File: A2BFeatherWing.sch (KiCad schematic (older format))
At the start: 2 parts, among them J1 Conn_01x04_Male, U1 FeatherWingTemplate

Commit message: added datasheets, power
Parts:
- U1: symbol Knochi_Modules:FeatherWingTemplate -> A2BFeatherWing-rescue:FeatherWingTemplate-Knochi_Modules
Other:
- note added: "* Feather M0 - either rx or tx\n * WS connected to pin 0 \n * CLK connected to pin 1\n * SD connected to pin 9"
- note added: "* Feather M4 - simultaneous rx and tx\n * WS connected to pin 0\n * CLK connected to pin 1\n * SDI connected to pin 12\n * SDO connected to pin 11"
- moved on the sheet: J1
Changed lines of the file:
@@
 $EndDescr
 $Comp
-L Knochi_Modules:FeatherWingTemplate U1
+L A2BFeatherWing-rescue:FeatherWingTemplate-Knochi_Modules U1
 U 1 1 5DC48552
 P 2000 6000
@@
 $EndComp
 $Sheet
-S 6200 2600 1450 1300
+S 5975 2725 1375 1650
 U 5DC4BC55
 F0 "A2B" 50
 F1 "A2BFeatherWing_A2B.sch" 50
+F2 "BN" O R 7350 3175 50
+F3 "BP" O R 7350 3275 50
+F4 "AN" O R 7350 3475 50
+F5 "AP" O R 7350 3375 50
+F6 "SCL" I L 5975 3000 50
+F7 "SDA" B L 5975 3125 50
+F8 "BCLK" I L 5975 3325 50
+F9 "SYNC" I L 5975 3450 50
+F10 "IO0" B L 5975 3575 50
+F11 "IO1" B L 5975 3650 50
+F12 "IO2" B L 5975 3750 50
+F13 "IO3" B L 5975 3800 50
+F14 "IO4" B L 5975 3925 50
+F15 "IO5" B L 5975 3900 50
+F16 "IO6" B L 5975 3975 50
+F17 "IO7" B L 5975 3850 50
 $EndSheet
 $Comp
 L Connector:Conn_01x04_Male J1
 U 1 1 5DC5628E
-P 9000 3250
-F 0 "J1" H 8972 3132 50  0000 R CNN
-F 1 "Conn_01x04_Male" H 8972 3223 50  0000 R CNN
-F 2 "Connector_JST:JST_PH_S4B-PH-SM4-TB_1x04-1MP_P2.00mm_Horizontal" H 9000 3250 50  0001 C CNN
-F 3 "~" H 9000 3250 50  0001 C CNN
-	1    9000 3250
+P 9000 3375
+F 0 "J1" H 8972 3257 50  0000 R CNN
+F 1 "Conn_01x04_Male" H 8972 3348 50  0000 R CNN
+F 2 "Connector_JST:JST_PH_S4B-PH-SM4-TB_1x04-1MP_P2.00mm_Horizontal" H 9000 3375 50  0001 C CNN
+F 3 "~" H 9000 3375 50  0001 C CNN
+	1    9000 3375
 	-1   0    0    1
 $EndComp
@@
 F1 "A2BFeatherWing_PWR.sch" 50
 $EndSheet
+Text Notes 2925 7100 0    50   ~ 0
+ * Feather M0 - either rx or tx\n   * WS connected to pin 0 \n   * CLK connected to pin 1\n   * SD connected to pin 9
+Text Notes 2975 6425 0    50   ~ 0
+* Feather M4 - simultaneous rx and tx\n  * WS connected to pin 0\n  * CLK connected to pin 1\n  * SDI connected to pin 12\n  * SDO connected to pin 11
 $EndSCHEMATC

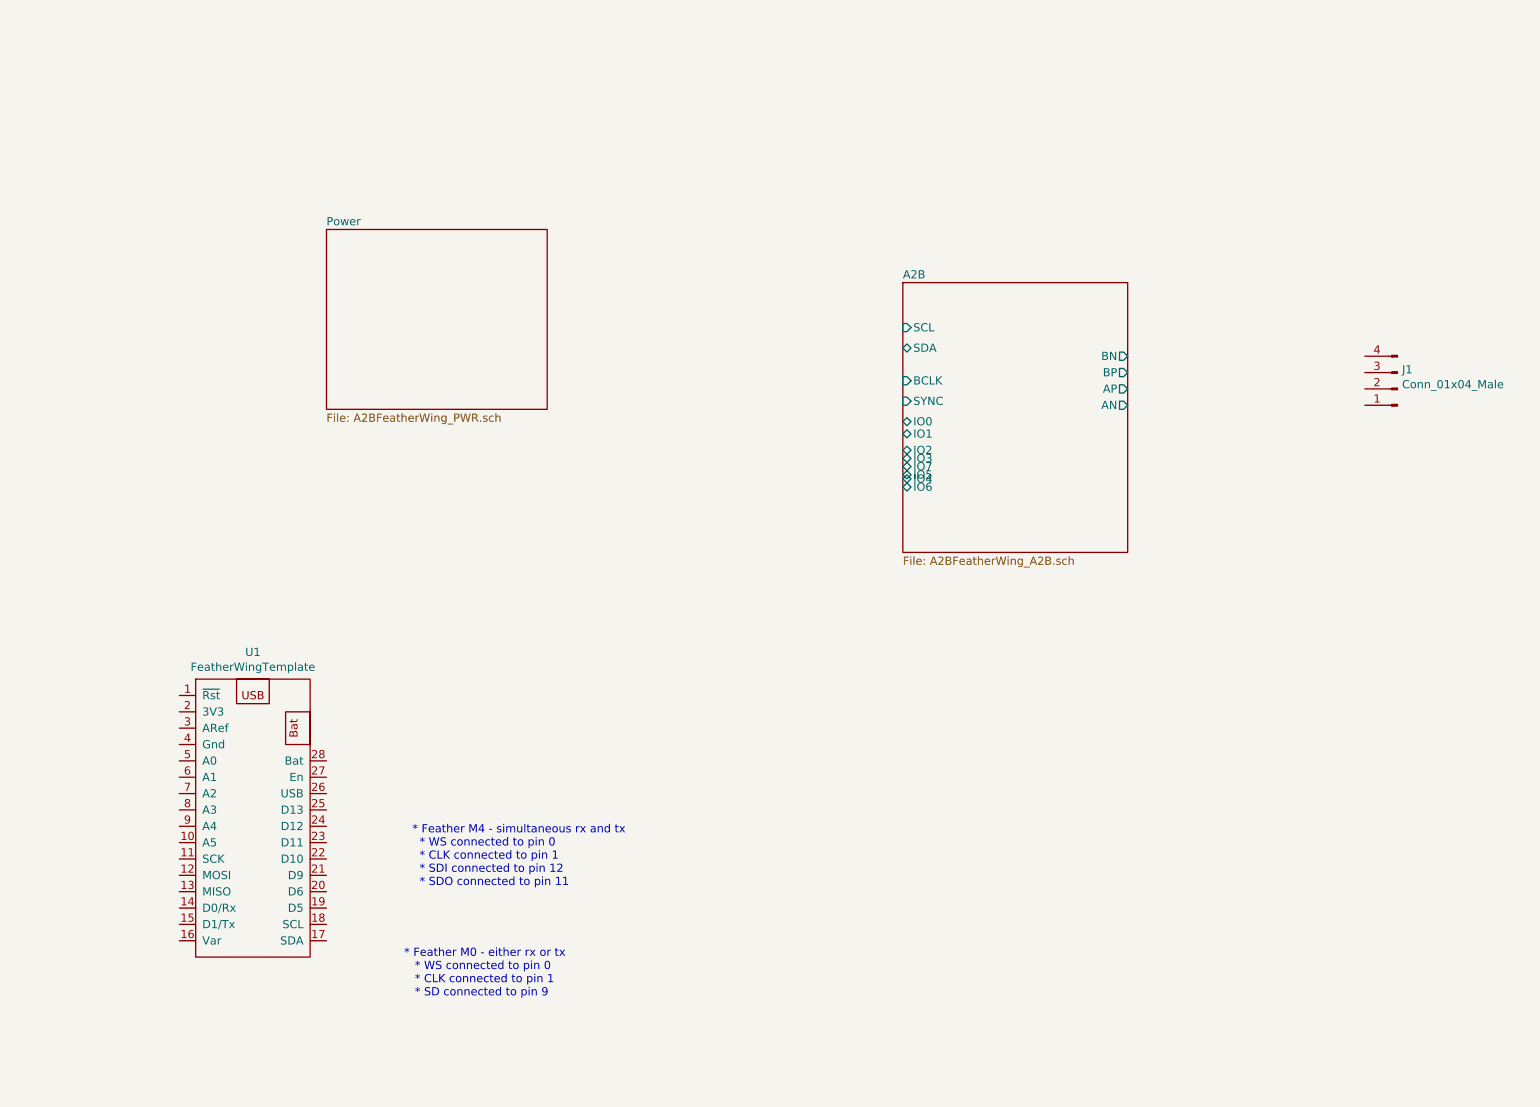
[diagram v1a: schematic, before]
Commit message: added 3d model of JST PH and CM added eco layer for silkscreen
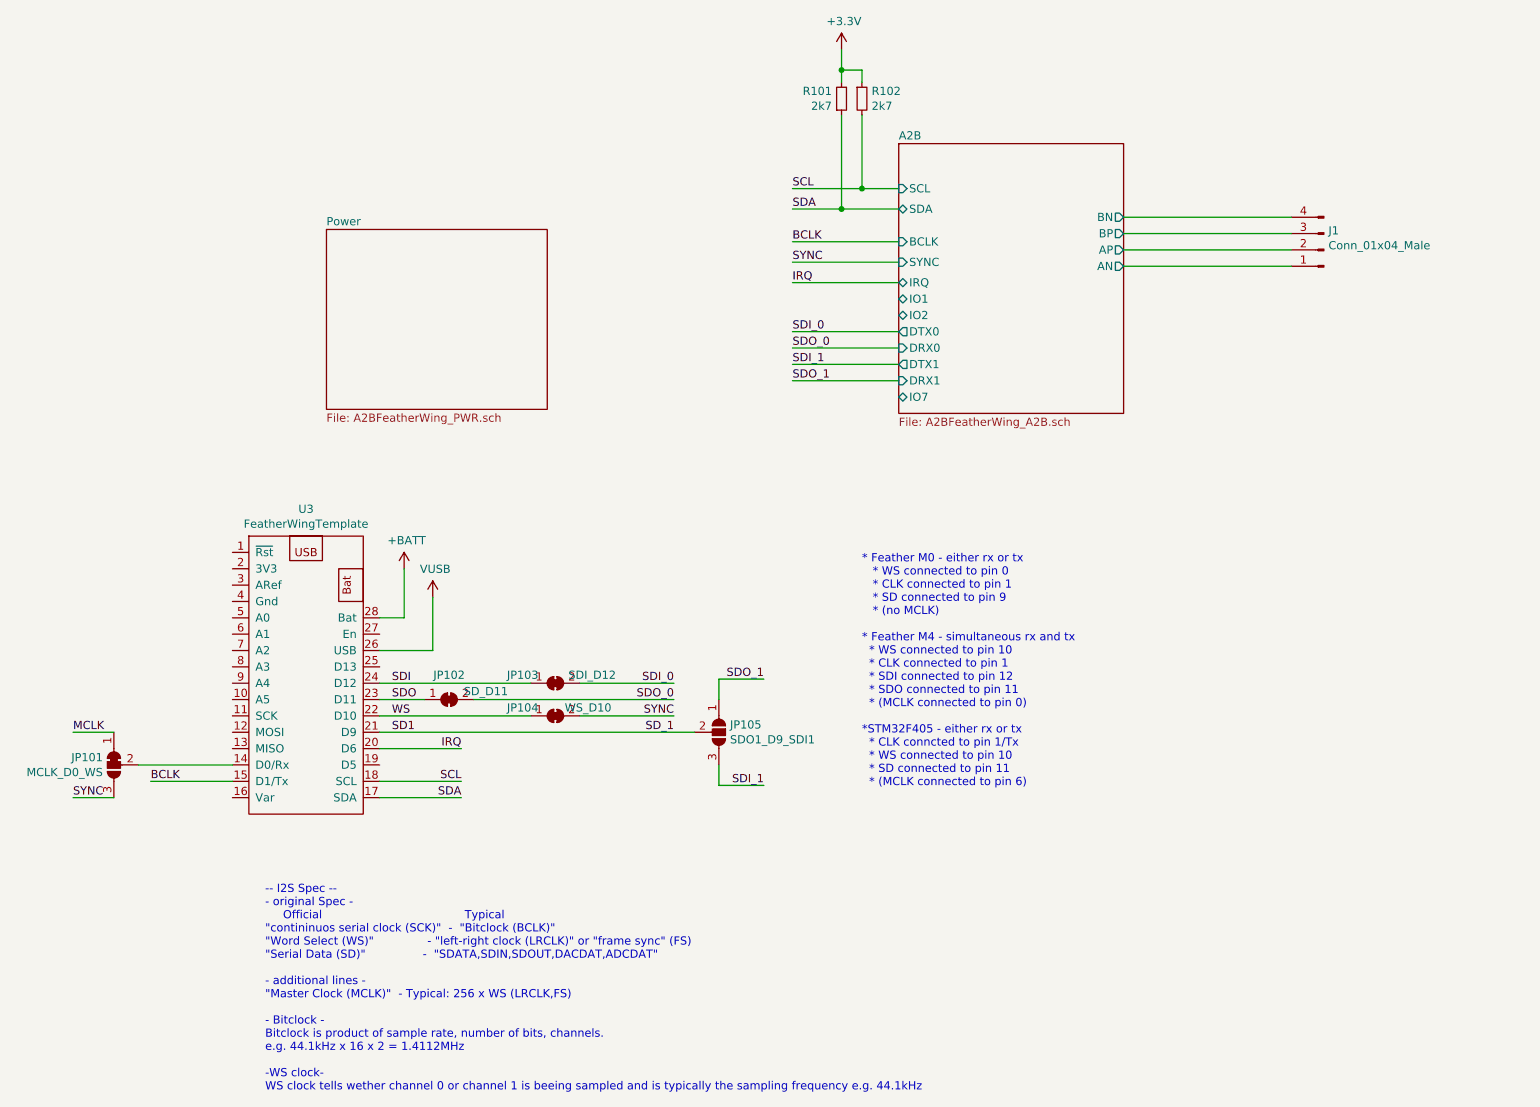
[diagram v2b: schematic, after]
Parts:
- added JP101: MCLK_D0_WS, Jumper:SolderJumper-3_P1.3mm_Bridged12_Pad1.0x1.5mm, symbol Jumper:SolderJumper_3_Bridged12
- added JP102: SD_D11, Jumper:SolderJumper-2_P1.3mm_Bridged_Pad1.0x1.5mm, symbol Jumper:SolderJumper_2_Bridged
- added JP103: SDI_D12, Jumper:SolderJumper-2_P1.3mm_Bridged_Pad1.0x1.5mm, symbol Jumper:SolderJumper_2_Bridged
- added JP104: WS_D10, Jumper:SolderJumper-2_P1.3mm_Bridged_Pad1.0x1.5mm, symbol Jumper:SolderJumper_2_Bridged
- added JP105: SDO1_D9_SDI1, Jumper:SolderJumper-3_P1.3mm_Open_Pad1.0x1.5mm, symbol Jumper:SolderJumper_3_Open
- added R101, R102: 2k7, Resistor_SMD:R_0402_1005Metric, symbol Device:R_Small
- renumbered U1 to U3
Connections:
- net A2B/AN: now also J1.1 (Pin_1)
- net A2B/AP: now also J1.2 (Pin_2)
- net A2B/BN: now also J1.4 (Pin_4)
- net A2B/BP: now also J1.3 (Pin_3)
- net at U3.14 (D0/Rx): now also JP101.2 (C)
- net BCLK: now reaches U3.15 (D1/Tx)
- net SDA: now reaches U3.17 (SDA)
- net SDA: now also R101.1
- net SCL: now reaches U3.18 (SCL)
- net SCL: now also R102.2
- net IRQ: now reaches U3.20 (D6)
- net SD1: now reaches U3.21 (D9)
- net SD1: now also JP105.2 (C)
- net WS: now reaches U3.22 (D10)
- net WS: now also JP104.1 (A)
- net SDO: now reaches U3.23 (D11)
- net SDO: now also JP102.1 (A)
- net SDI: now reaches U3.24 (D12)
- net SDI: now also JP103.1 (A)
- net VUSB: now reaches U3.26 (USB)
- net +BATT: now reaches U3.28 (Bat)
- new net +3V3: R101.2, R102.1
- new net MCLK: JP101.1 (A)
- new net SDI_0: JP103.2 (B)
- new net SDI_1: JP105.3 (B)
- new net SDO_0: JP102.2 (B)
- new net SDO_1: JP105.1 (A)
- new net SYNC: JP101.3 (B), JP104.2 (B)
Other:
- note added: "* Feather M0 - either rx or tx\n * WS connected to pin 0 \n * CLK connected to pin 1\n * SD connected to pin 9 \n * (no MCLK)\n\n* Feather M4 - simultaneous rx and tx\n * WS connected to pin 10\n * CLK connected to pin 1\n * SDI connected to pin 12\n * SDO connected to pin 11\n * (MCLK connected to pin 0)\n\n*STM32F405 - either rx or tx\n * CLK conncted to pin 1/Tx\n * WS connected to pin 10\n * 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"
- note added: "-- I2S Spec --\n- original Spec -\n Official Typical\n"contininuos serial clock (SCK)" - "Bitclock (BCLK)"\n"Word Select (WS)" - "left-right clock (LRCLK)" or "frame sync" (FS)\n"Serial Data (SD)" - "SDATA,SDIN,SDOUT,DACDAT,ADCDAT"\n\n- additional lines -\n"Master Clock (MCLK)" - Typical: 256 x WS (LRCLK,FS)\n\n- Bitclock -\nBitclock is product of sample rate, number of bits, channels.\ne.g. 44.1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"
- note removed: "* Feather M0 - either rx or tx\n * WS connected to pin 0 \n * CLK connected to pin 1\n * SD connected to pin 9"
- note removed: "* Feather M4 - simultaneous rx and tx\n * WS connected to pin 0\n * CLK connected to pin 1\n * SDI connected to pin 12\n * SDO connected to pin 11"
- moved on the sheet: J1, U3

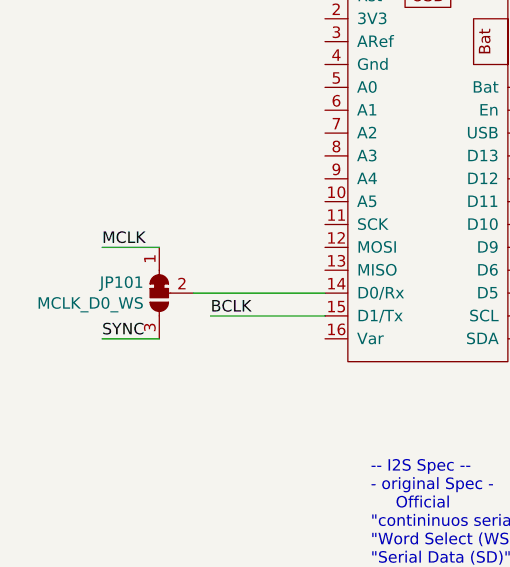
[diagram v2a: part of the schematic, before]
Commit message: - added documentation - removed MCLK
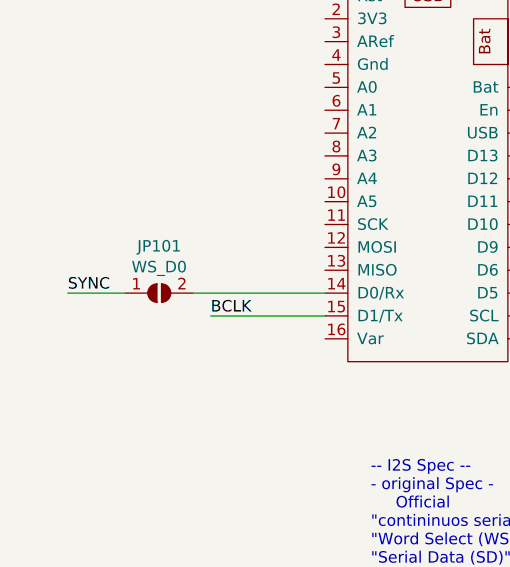
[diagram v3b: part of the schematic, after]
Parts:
- removed JP101: MCLK_D0_WS, Jumper:SolderJumper-3_P1.3mm_Bridged12_Pad1.0x1.5mm, symbol Jumper:SolderJumper_3_Bridged12
- added JP101: WS_D0, Jumper:SolderJumper-2_P1.3mm_Open_Pad1.0x1.5mm, symbol Jumper:SolderJumper_2_Open
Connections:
- net SYNC: now also JP101.1 (A)
- net at U3.14 (D0/Rx): now also JP101.2 (B)
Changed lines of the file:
@@
 	5300 2475 5950 2475
 Wire Wire Line
-	1150 5875 900  5875
-Text Label 900  5875 0    50   ~ 0
+	1000 5675 750  5675
+Text Label 750  5675 0    50   ~ 0
 SYNC
 $Comp
@@
 Wire Wire Line
 	3700 5175 2775 5175
-Text Label 900  5475 0    50   ~ 0
-MCLK
-Wire Wire Line
-	900  5475 1150 5475
-$Comp
-L Jumper:SolderJumper_3_Bridged12 JP101
-U 1 1 5DF1F036
-P 1150 5675
-F 0 "JP101" V 1104 5743 50  0000 L CNN
-F 1 "MCLK_D0_WS" V 1195 5743 50  0000 L CNN
-F 2 "Jumper:SolderJumper-3_P1.3mm_Bridged12_Pad1.0x1.5mm" H 1150 5675 50  0001 C CNN
-F 3 "~" H 1150 5675 50  0001 C CNN
-	1    1150 5675
-	0    -1   1    0
-$EndComp
 Wire Wire Line
 	1300 5675 1875 5675
@@
 Text Label 2850 5475 0    50   ~ 0
 SD1
+$Comp
+L Jumper:SolderJumper_2_Open JP101
+U 1 1 5DF90C87
+P 1150 5675
+F 0 "JP101" H 1150 5880 50  0000 C CNN
+F 1 "WS_D0" H 1150 5789 50  0000 C CNN
+F 2 "Jumper:SolderJumper-2_P1.3mm_Open_Pad1.0x1.5mm" H 1150 5675 50  0001 C CNN
+F 3 "~" H 1150 5675 50  0001 C CNN
+	1    1150 5675
+	1    0    0    -1
+$EndComp
 $EndSCHEMATC
